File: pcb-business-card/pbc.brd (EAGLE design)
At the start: 50 x 88 mm, 27 parts, among them IC1 NET2272REV1A-BCF, J1 CON2, U1 MEGA32U4-MU, U2 RT9193-33GB, U5 TMP117AIYBGR

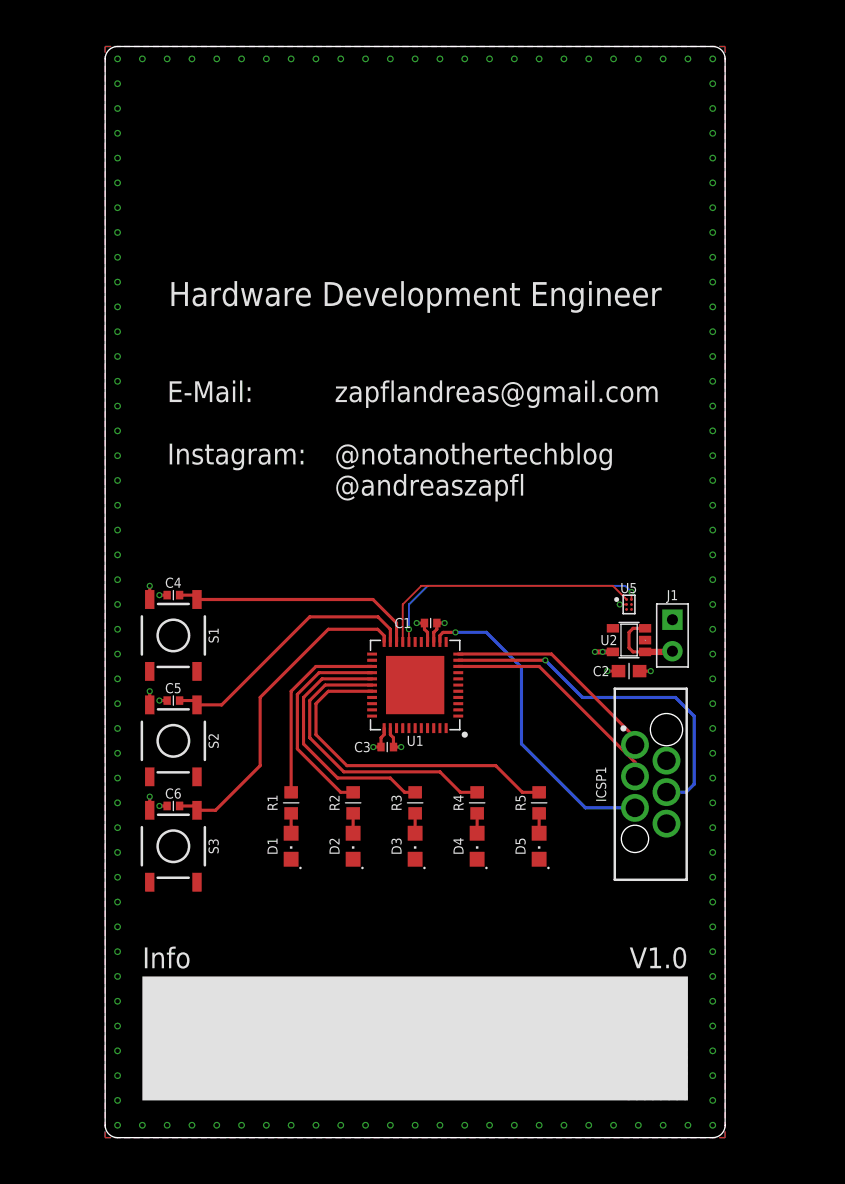
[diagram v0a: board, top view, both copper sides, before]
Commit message: Added instagram and mail logo
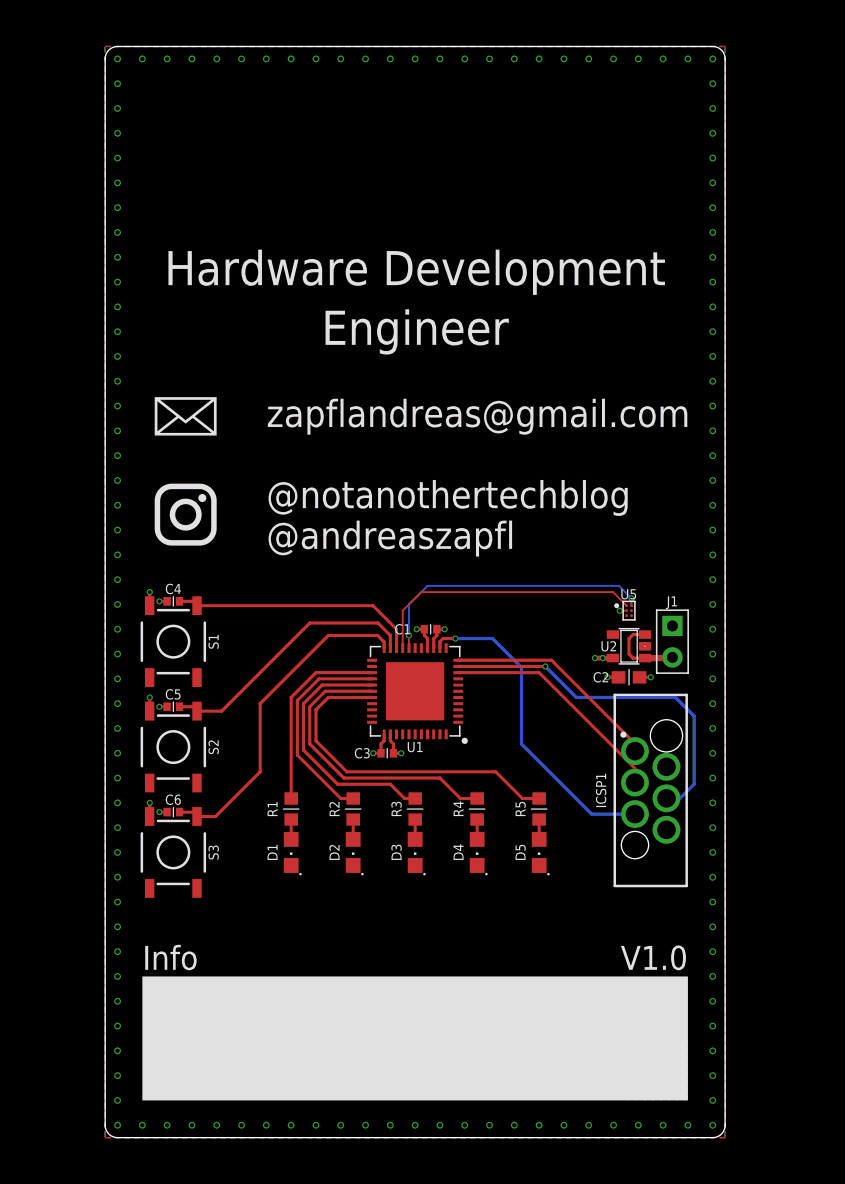
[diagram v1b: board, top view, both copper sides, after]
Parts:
- added U$2: (no value), zaan-Symbols:INSTA-5
- added U$3: (no value), zaan-Symbols:MAIL-5
- moved C1 0.50 mm to (26.2, 41.0)
- moved C2 0.50 mm to (42.2, 37.1)
- moved C3 0.50 mm to (22.8, 31.0)
- moved C4 0.50 mm to (5.50, 43.2)
- moved C5 0.50 mm to (5.50, 34.8)
- moved C6 0.50 mm to (5.50, 26.2)
- moved D1 0.50 mm to (15.0, 23.0)
- moved D2 0.50 mm to (20.0, 23.0)
- moved D3 0.50 mm to (25.0, 23.0)
- moved D4 0.50 mm to (30.0, 23.0)
- moved D5 0.50 mm to (35.0, 23.0)
- moved ICSP1 0.50 mm to (44.0, 28.0)
- moved J1 0.50 mm to (45.8, 40.0)
- moved R1 0.50 mm to (15.0, 26.5)
- moved R2 0.50 mm to (20.0, 26.5)
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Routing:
- net ISCL: track 22.4 -> 23.1 mm
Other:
- board text removed: "E-Mail: Instagram:"

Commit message: Created gerbers
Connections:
- net PB6(PCINT6/OC1B/OC4B/ADC13) renamed PB6
- net PB7(PCINT7/OC0A/OC1C/!RTS!) renamed PB7
- net PC6(OC3A/!OC4A!) renamed PC6
- net PC7(ICP3/CLK0/OC4A) renamed PC7
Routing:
- net SCK: track 18.6 -> 17.9 mm
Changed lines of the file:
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@@
 <setting verticaltext="up"/>
 </settings>
-<grid distance="0.5" unitdist="mm" unit="mm" style="lines" multiple="1" display="yes" altdistance="0.125" altunitdist="mm" altunit="mm"/>
+<grid distance="0.5" unitdist="mm" unit="mm" style="lines" multiple="1" display="yes" altdistance="0.25" altunitdist="mm" altunit="mm"/>
 <layers>
 <layer number="1" name="Top" color="4" fill="1" visible="yes" active="yes"/>
-<layer number="2" name="Route2" color="16" fill="1" visible="no" active="yes"/>
+<layer number="2" name="Route2" color="16" fill="1" visible="no" active="no"/>
 <layer number="3" name="Route3" color="17" fill="1" visible="no" active="no"/>
 <layer number="4" name="Route4" color="18" fill="1" visible="no" active="no"/>
@@
 <layer number="13" name="Route13" color="21" fill="1" visible="no" active="no"/>
 <layer number="14" name="Route14" color="22" fill="1" visible="no" active="no"/>
-<layer number="15" name="Route15" color="23" fill="1" visible="no" active="yes"/>
-<layer number="16" name="Bottom" color="1" fill="1" visible="no" active="yes"/>
+<layer number="15" name="Route15" color="23" fill="1" visible="no" active="no"/>
+<layer number="16" name="Bottom" color="1" fill="1" visible="yes" active="yes"/>
 <layer number="17" name="Pads" color="2" fill="1" visible="yes" active="yes"/>
 <layer number="18" name="Vias" color="2" fill="1" visible="yes" active="yes"/>
@@
 <layer number="20" name="Dimension" color="13" fill="1" visible="yes" active="yes"/>
 <layer number="21" name="tPlace" color="7" fill="1" visible="yes" active="yes"/>
-<layer number="22" name="bPlace" color="7" fill="1" visible="no" active="yes"/>
+<layer number="22" name="bPlace" color="7" fill="1" visible="yes" active="yes"/>
 <layer number="23" name="tOrigins" color="15" fill="1" visible="yes" active="yes"/>
-<layer number="24" name="bOrigins" color="15" fill="1" visible="no" active="yes"/>
+<layer number="24" name="bOrigins" color="15" fill="1" visible="yes" active="yes"/>
 <layer number="25" name="tNames" color="7" fill="1" visible="yes" active="yes"/>
-<layer number="26" name="bNames" color="7" fill="1" visible="no" active="yes"/>
+<layer number="26" name="bNames" color="7" fill="1" visible="yes" active="yes"/>
 <layer number="27" name="tValues" color="7" fill="1" visible="no" active="yes"/>
 <layer number="28" name="bValues" color="7" fill="1" visible="no" active="yes"/>
-<layer number="29" name="tStop" color="7" fill="3" visible="no" active="yes"/>
+<layer number="29" name="tStop" color="7" fill="3" visible="yes" active="yes"/>
 <layer number="30" name="bStop" color="7" fill="6" visible="no" active="yes"/>
 <layer number="31" name="tCream" color="7" fill="4" visible="no" active="yes"/>
@@
 <layer number="38" name="bTest" color="7" fill="1" visible="no" active="yes"/>
 <layer number="39" name="tKeepout" color="4" fill="11" visible="yes" active="yes"/>
-<layer number="40" name="bKeepout" color="1" fill="11" visible="no" active="yes"/>
+<layer number="40" name="bKeepout" color="1" fill="11" visible="yes" active="yes"/>
 <layer number="41" name="tRestrict" color="4" fill="10" visible="yes" active="yes"/>
-<layer number="42" name="bRestrict" color="1" fill="10" visible="no" active="yes"/>
+<layer number="42" name="bRestrict" color="1" fill="10" visible="yes" active="yes"/>
 <layer number="43" name="vRestrict" color="2" fill="10" visible="no" active="yes"/>
 <layer number="44" name="Drills" color="7" fill="1" visible="no" active="yes"/>
@@
 <layer number="50" name="dxf" color="7" fill="1" visible="no" active="no"/>
 <layer number="51" name="tDocu" color="14" fill="1" visible="yes" active="yes"/>
-<layer number="52" name="bDocu" color="15" fill="1" visible="no" active="yes"/>
+<layer number="52" name="bDocu" color="15" fill="1" visible="yes" active="yes"/>
 <layer number="53" name="tGND_GNDA" color="7" fill="9" visible="no" active="no"/>
 <layer number="54" name="bGND_GNDA" color="1" fill="9" visible="no" active="no"/>
@@
 <text x="47" y="14.5" size="1.9304" layer="25" font="vector" ratio="15" rot="R180" align="center-left">V1.0</text>
 <text x="4" y="59.5" size="1.6764" layer="25" font="vector" ratio="15" distance="75" align="top-left"></text>
-<text x="13" y="59.5" size="2.1844" layer="25" font="vector" ratio="15" align="top-left">zapflandreas@gmail.com
+<text x="12.5" y="59.5" size="2.1844" layer="25" font="vector" ratio="15" align="top-left">zapflandreas@gmail.com
 @notanothertechblog
 @andreaszapfl</text>
@@
 </class>
 </classes>
-<designrules name="Multi-CB_4L_EET">
+<designrules name="Multi-CB_4L_EET *">
 <description language="de">&lt;b&gt;Multi-CB EAGLE Design Rules für 4 Lagen Standard (ohne Aufpreis)&lt;/b&gt;
 &lt;br&gt;
@@
 &lt;em&gt;All statements without guarantee! A perfect setting of design rules can understandably only be performed by the user.&lt;/em&gt;
 &lt;/p&gt;</description>
-<param name="layerSetup" value="(1+2*15+16)"/>
+<param name="layerSetup" value="(1*16)"/>
 <param name="mtCopper" value="0.035mm 0.018mm 0.035mm 0.035mm 0.035mm 0.035mm 0.035mm 0.035mm 0.035mm 0.035mm 0.035mm 0.035mm 0.035mm 0.035mm 0.018mm 0.035mm"/>
-<param name="mtIsolate" value="0.36mm 0.71mm 0.36mm 0.2mm 0.2mm 0.2mm 0.2mm 0.15mm 0.2mm 0.15mm 0.2mm 0.15mm 0.2mm 0.15mm 0.36mm"/>
+<param name="mtIsolate" value="1.44mm 0.71mm 0.36mm 0.2mm 0.2mm 0.2mm 0.2mm 0.15mm 0.2mm 0.15mm 0.2mm 0.15mm 0.2mm 0.15mm 0.36mm"/>
 <param name="mdWireWire" value="0.1mm"/>
 <param name="mdWirePad" value="0.1mm"/>
@@
 <contactref element="ICSP1" pad="1"/>
 <contactref element="U1" pad="11"/>
-<wire x1="36" y1="38.5" x2="28.475" y2="38.5" width="0.254" layer="1"/>
-<wire x1="42.73" y1="31.175" x2="42.73" y2="31.77" width="0.254" layer="1"/>
-<wire x1="42.73" y1="31.77" x2="36" y2="38.5" width="0.254" layer="1"/>
+<wire x1="35.405" y1="38.5" x2="28.475" y2="38.5" width="0.254" layer="1"/>
+<wire x1="42.73" y1="31.175" x2="35.405" y2="38.5" width="0.254" layer="1"/>
 </signal>
 <signal name="SCK">
 <contactref element="ICSP1" pad="3"/>
 <contactref element="U1" pad="9"/>
-<wire x1="35" y1="37.5" x2="28.475" y2="37.5" width="0.254" layer="1"/>
-<wire x1="42.73" y1="28.635" x2="42.73" y2="29.77" width="0.254" layer="1"/>
-<wire x1="42.73" y1="29.77" x2="35" y2="37.5" width="0.254" layer="1"/>
+<wire x1="42.73" y1="28.635" x2="33.865" y2="37.5" width="0.254" layer="1"/>
+<wire x1="33.865" y1="37.5" x2="28.475" y2="37.5" width="0.254" layer="1"/>
 </signal>
 <signal name="RST">
@@
 <wire x1="27.25" y1="40.25" x2="28.25" y2="40.25" width="0.254" layer="1"/>
 <via x="28.25" y="40.25" extent="1-16" drill="0.3"/>
-<wire x1="33.575" y1="37.925" x2="31.25" y2="40.25" width="0.254" layer="16"/>
-<wire x1="28.25" y1="40.25" x2="31.25" y2="40.25" width="0.254" layer="16"/>
-<wire x1="33.575" y1="37.925" x2="33.575" y2="31.75" width="0.254" layer="16"/>
+<wire x1="32.575" y1="38.425" x2="30.75" y2="40.25" width="0.254" layer="16"/>
+<wire x1="28.25" y1="40.25" x2="30.75" y2="40.25" width="0.254" layer="16"/>
+<wire x1="32.575" y1="38.425" x2="32.575" y2="32.75" width="0.254" layer="16"/>
 <wire x1="42.73" y1="26.095" x2="39.23" y2="26.095" width="0.254" layer="16"/>
-<wire x1="39.23" y1="26.095" x2="33.575" y2="31.75" width="0.254" layer="16"/>
+<wire x1="39.23" y1="26.095" x2="32.575" y2="32.75" width="0.254" layer="16"/>
 </signal>
 <signal name="MOSI">
 <contactref element="ICSP1" pad="4"/>
 <contactref element="U1" pad="10"/>
-<wire x1="28.475" y1="38" x2="35.5" y2="38" width="0.254" layer="1"/>
-<via x="35.5" y="38" extent="1-16" drill="0.3"/>
+<wire x1="28.475" y1="38" x2="34.625" y2="38" width="0.254" layer="1"/>
+<via x="34.625" y="38" extent="1-16" drill="0.3"/>
 <wire x1="46" y1="35.5" x2="47.5" y2="34" width="0.254" layer="16"/>
 <wire x1="46.365" y1="27.365" x2="45.27" y2="27.365" width="0.254" layer="16"/>
-<wire x1="46" y1="35.5" x2="38" y2="35.5" width="0.254" layer="16"/>
-<wire x1="35.5" y1="38" x2="38" y2="35.5" width="0.254" layer="16"/>
+<wire x1="46" y1="35.5" x2="37.125" y2="35.5" width="0.254" layer="16"/>
+<wire x1="34.625" y1="38" x2="37.125" y2="35.5" width="0.254" layer="16"/>
 <wire x1="47.5" y1="34" x2="47.5" y2="28.5" width="0.254" layer="16"/>
 <wire x1="47.5" y1="28.5" x2="46.365" y2="27.365" width="0.254" layer="16"/>
 </signal>
-<signal name="PC7(ICP3/CLK0/OC4A)">
+<signal name="PC7">
 <contactref element="U1" pad="32"/>
 </signal>
@@
 <contactref element="U1" pad="3"/>
 </signal>
-<signal name="PC6(OC3A/!OC4A!)">
+<signal name="PC6">
 <contactref element="U1" pad="31"/>
 </signal>
-<signal name="PB6(PCINT6/OC1B/OC4B/ADC13)">
+<signal name="PB6">
 <contactref element="U1" pad="30"/>
 </signal>
@@
 <contactref element="U1" pad="16"/>
 </signal>
-<signal name="PB7(PCINT7/OC0A/OC1C/!RTS!)">
+<signal name="PB7">
 <contactref element="U1" pad="12"/>
 </signal>

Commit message: Black substrate change
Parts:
- moved U$2 2.25 mm to (6.25, 47.8)
- moved U$3 2.25 mm to (6.25, 56.6)
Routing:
- net GND: track 10.9 -> 316.4 mm, vias 143 -> 150
- net VCC: track 7.69 -> 54.9 mm, vias 6 -> 5
- added copper zone on layer 16, net GND
- removed copper zone on layer 1, net GND
- removed copper zone on layer 16, net VCC
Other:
- board text added: "50 to 87 line space (deleted second tag @)"
- board text added: "This is a test"
- board text added: "V1.0B"
- board text added: "mail@address @notanothertechblog"
- board text removed: "Andreas Zapfl"
- board text removed: "V1.0"
- board text removed: "zapflandreas@gmail.com @notanothertechblog @andreaszapfl"
